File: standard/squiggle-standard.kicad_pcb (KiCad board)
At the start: 2 copper layers, 116 x 115.3 mm, 36 parts, among them SW1 switch, SW10 switch, SW11 switch, SW12 switch, SW13 switch, SW14 switch, SW15 switch, SW16 switch, SW17 switch, SW2 switch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

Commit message: minor thumb adjustments
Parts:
- SW13, SW17: footprint footprints:2u-dual -> footprints:1u-minimal
- moved D13 14.1 mm to (104.4, 88.0), turned to 73.4 degrees
- moved D17 13.9 mm to (110.1, 89.8)
- moved SW17 12.0 mm to (115.8, 95.5), turned to -26.6 degrees
- moved SW13 10.8 mm to (96.5, 87.9), turned to -16.6 degrees
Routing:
- removed copper zone on B.Cu, net (none)
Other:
- net class Default removed

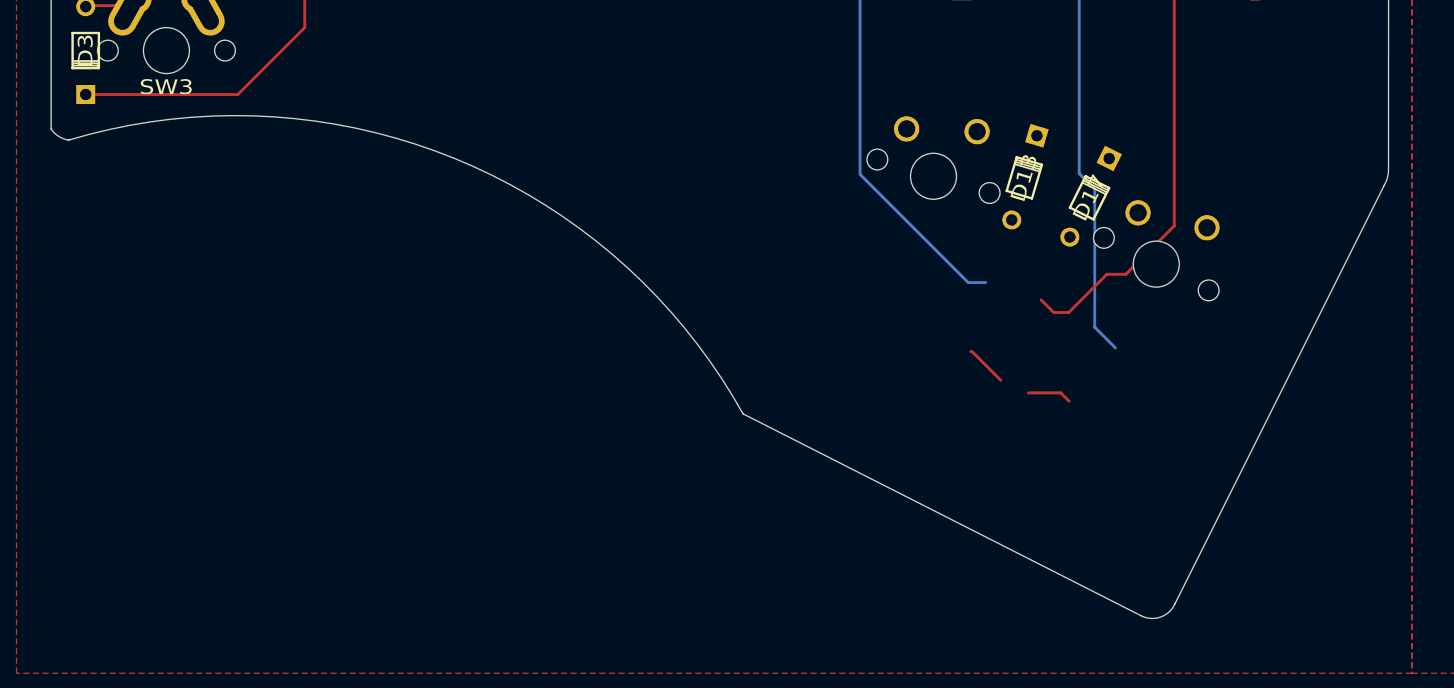
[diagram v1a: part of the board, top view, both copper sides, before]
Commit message: added placeholder for rotary encoder, swapped diodes orientations
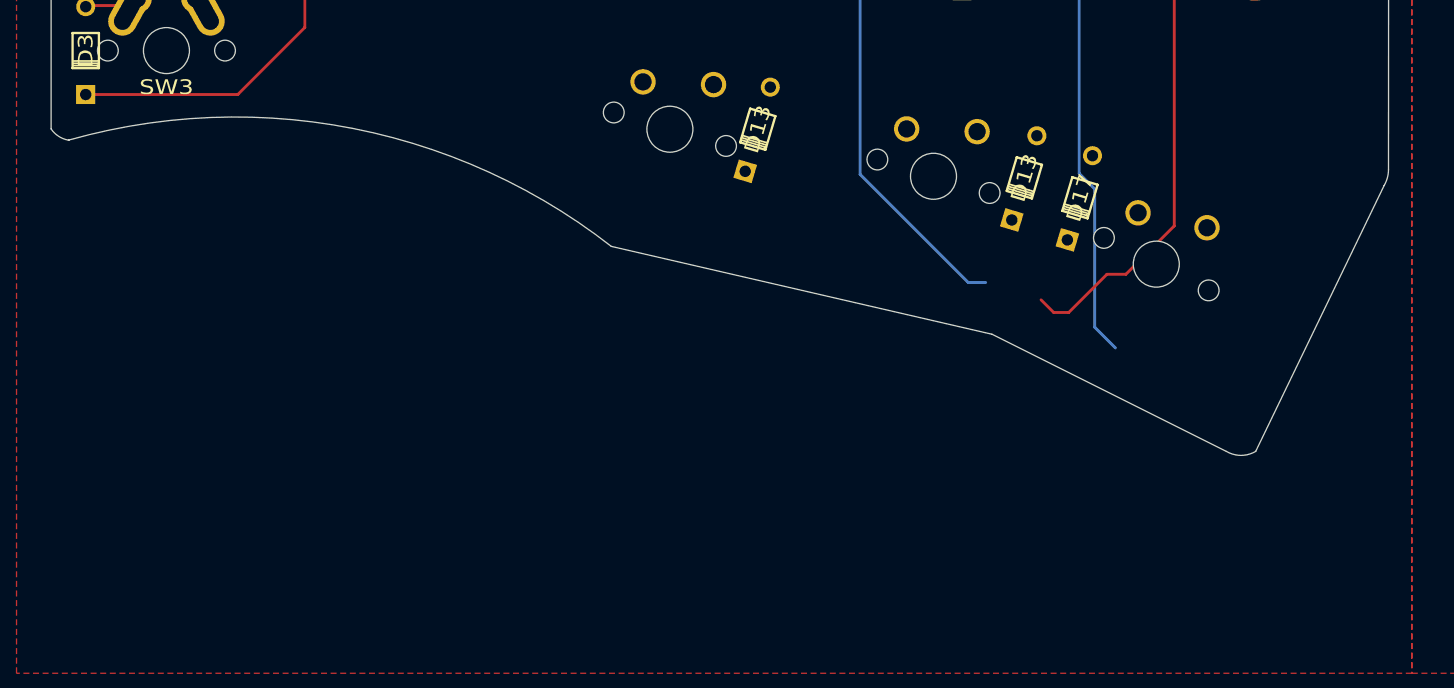
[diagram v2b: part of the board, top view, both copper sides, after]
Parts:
- added D13: D, footprints:diode, F.Cu at (81.3, 83.8)
- added SW13: switch, footprints:1u-minimal, F.Cu at (73.7, 83.8)
- moved D17 0.83 mm to (109.2, 89.8), turned to -106.6 degrees
- turned D13 to -106.6 degrees
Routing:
- net Net-(D17-Pad2): track 3.83 -> 0.00 mm
- net Net-(D13-Pad2): track 3.63 -> 0.00 mm
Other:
- board size 116 x 115.3 mm -> 116 x 101.2 mm
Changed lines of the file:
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@@
   )
   (footprint "footprints:diode" (layer "F.Cu")
-    (at 104.397119 88.037509 73.4)
+    (at 104.397119 88.037509 -106.6)
     (attr through_hole)
     (fp_text reference "D13" (at 0 0 73.4) (layer "F.SilkS")
@@
     (fp_line (start 1.3 1.1) (end 1.3 -1) (layer "F.SilkS") (width 0.15))
     (fp_line (start 0.9 1.1) (end 0.9 -1.1) (layer "F.SilkS") (width 0.15))
-    (pad "1" thru_hole rect locked (at 3.81 0 73.4) (size 1.651 1.651) (drill 0.9906) (layers *.Cu *.SilkS *.Mask)
+    (pad "1" thru_hole rect locked (at 3.81 0 253.4) (size 1.651 1.651) (drill 0.9906) (layers *.Cu *.SilkS *.Mask)
       (net 15 "ROW3"))
-    (pad "2" thru_hole circle locked (at -3.81 0 73.4) (size 1.651 1.651) (drill 0.9906) (layers *.Cu *.SilkS *.Mask)
+    (pad "2" thru_hole circle locked (at -3.81 0 253.4) (size 1.651 1.651) (drill 0.9906) (layers *.Cu *.SilkS *.Mask)
       (net 26 "Net-(D13-Pad2)"))
   )
   (footprint "footprints:diode" (layer "F.Cu")
-    (at 110.054038 89.766728 63.4)
-    (attr through_hole)
-    (fp_text reference "D17" (at 0 0 63.4) (layer "F.SilkS")
-      (effects (font (size 1.27 1.524) (thickness 0.2032)))
-    )
-    (fp_text value "D" (at 0 0 63.4) (layer "F.SilkS") hide
+    (at 109.22 89.766728 -106.6)
+    (attr through_hole)
+    (fp_text reference "D17" (at 0 0 73.4) (layer "F.SilkS")
+      (effects (font (size 1.27 1.524) (thickness 0.2032)))
+    )
+    (fp_text value "D" (at 0 0 73.4) (layer "F.SilkS") hide
       (effects (font (size 1.27 1.524) (thickness 0.2032)))
     )
@@
     (fp_line (start -1.524 -1.143) (end 1.524 -1.143) (layer "F.SilkS") (width 0.2032))
     (fp_line (start 0.9 1.1) (end 0.9 -1.1) (layer "F.SilkS") (width 0.15))
-    (pad "1" thru_hole rect locked (at 3.81 0 63.4) (size 1.651 1.651) (drill 0.9906) (layers *.Cu *.SilkS *.Mask)
+    (pad "1" thru_hole rect locked (at 3.81 0 253.4) (size 1.651 1.651) (drill 0.9906) (layers *.Cu *.SilkS *.Mask)
       (net 15 "ROW3"))
-    (pad "2" thru_hole circle locked (at -3.81 0 63.4) (size 1.651 1.651) (drill 0.9906) (layers *.Cu *.SilkS *.Mask)
+    (pad "2" thru_hole circle locked (at -3.81 0 253.4) (size 1.651 1.651) (drill 0.9906) (layers *.Cu *.SilkS *.Mask)
       (net 13 "Net-(D17-Pad2)"))
   )
@@
     (pad "2" thru_hole circle locked (at -3.81 0 270) (size 1.651 1.651) (drill 0.9906) (layers *.Cu *.SilkS *.Mask)
       (net 11 "Net-(D15-Pad2)"))
+  )
+  (footprint "footprints:1u-minimal" (layer "F.Cu")
+    (at 73.66 83.82 -16.6)
+    (attr through_hole)
+    (fp_text reference "SW13" (at 0 4 163.4) (layer "F.SilkS") hide
+      (effects (font (size 1.27 1.524) (thickness 0.2032)))
+    )
+    (fp_text value "switch" (at 0 5.8 163.4) (layer "F.SilkS") hide
+      (effects (font (size 1.27 1.524) (thickness 0.2032)))
+    )
+    (fp_text user "2.00u" (at -15.24 8.255 163.4) (layer "Dwgs.User")
+      (effects (font (size 1.524 1.524) (thickness 0.3048)))
+    )
+    (fp_line (start 9.5 9.5) (end -9.5 9.5) (layer "Dwgs.User") (width 0.1))
+    (fp_line (start -9.5 -9.5) (end 9.5 -9.5) (layer "Dwgs.User") (width 0.1))
+    (fp_line (start 9.5 -9.5) (end 9.5 9.5) (layer "Dwgs.User") (width 0.1))
+    (fp_line (start -9.5 9.5) (end -9.5 -9.5) (layer "Dwgs.User") (width 0.1))
+    (pad "" np_thru_hole circle locked (at 5.08 0 343.4) (size 1.8 1.8) (drill 1.8) (layers *.Cu *.Mask))
+    (pad "" np_thru_hole circle locked (at 0 0 343.4) (size 3.9878 3.9878) (drill 3.9878) (layers *.Cu *.Mask))
+    (pad "" np_thru_hole circle locked (at -5.08 0 343.4) (size 1.8 1.8) (drill 1.8) (layers *.Cu *.Mask))
+    (pad "1" thru_hole circle locked (at -3.405 -3.27 12.4) (size 2.2 2.2) (drill 1.5) (layers *.Cu *.Mask))
+    (pad "2" thru_hole circle locked (at 2.52 -4.79 343.4) (size 2.2 2.2) (drill 1.5) (layers *.Cu *.Mask))
+  )
+  (footprint "footprints:diode" (layer "F.Cu")
+    (at 81.28 83.82 -106.6)
+    (attr through_hole)
+    (fp_text reference "D13" (at 0 0 73.4) (layer "F.SilkS")
+      (effects (font (size 1.27 1.524) (thickness 0.2032)))
+    )
+    (fp_text value "D" (at 0 0 73.4) (layer "F.SilkS") hide
+      (effects (font (size 1.27 1.524) (thickness 0.2032)))
+    )
+    (fp_line (start 1.524 1.143) (end -1.524 1.143) (layer "B.SilkS") (width 0.2032))
+    (fp_line (start 1.524 -1.143) (end 1.524 1.143) (layer "B.SilkS") (width 0.2032))
+    (fp_line (start -1.524 -1.143) (end 1.524 -1.143) (layer "B.SilkS") (width 0.2032))
+    (fp_line (start 1.3 -1) (end 1.3 -1.1) (layer "B.SilkS") (width 0.15))
+    (fp_line (start 1.3 -1.1) (end 1.3 -1) (layer "B.SilkS") (width 0.15))
+    (fp_line (start 1.1 -1.1) (end 1.1 1.1) (layer "B.SilkS") (width 0.15))
+    (fp_line (start 0.9 1.1) (end 0.9 -1.1) (layer "B.SilkS") (width 0.15))
+    (fp_line (start 1.3 1.1) (end 1.3 -1) (layer "B.SilkS") (width 0.15))
+    (fp_line (start -1.524 1.143) (end -1.524 -1.143) (layer "B.SilkS") (width 0.2032))
+    (fp_line (start 1.524 -1.143) (end 1.524 1.143) (layer "F.SilkS") (width 0.2032))
+    (fp_line (start -1.524 -1.143) (end 1.524 -1.143) (layer "F.SilkS") (width 0.2032))
+    (fp_line (start 1.3 -1) (end 1.3 -1.1) (layer "F.SilkS") (width 0.15))
+    (fp_line (start -1.524 1.143) (end -1.524 -1.143) (layer "F.SilkS") (width 0.2032))
+    (fp_line (start 1.524 1.143) (end -1.524 1.143) (layer "F.SilkS") (width 0.2032))
+    (fp_line (start 1.1 -1.1) (end 1.1 1.1) (layer "F.SilkS") (width 0.15))
+    (fp_line (start 1.3 -1.1) (end 1.3 -1) (layer "F.SilkS") (width 0.15))
+    (fp_line (start 1.3 1.1) (end 1.3 -1) (layer "F.SilkS") (width 0.15))
+    (fp_line (start 0.9 1.1) (end 0.9 -1.1) (layer "F.SilkS") (width 0.15))
+    (pad "1" thru_hole rect locked (at 3.81 0 253.4) (size 1.651 1.651) (drill 0.9906) (layers *.Cu *.SilkS *.Mask))
+    (pad "2" thru_hole circle locked (at -3.81 0 253.4) (size 1.651 1.651) (drill 0.9906) (layers *.Cu *.SilkS *.Mask))
   )
   (footprint "footprints:trrs" (layer "B.Cu")
@@
   (gr_arc (start 21.499802 84.76712) (mid 20.652379 84.434796) (end 20.000001 83.799999) (layer "Edge.Cuts") (width 0.05))
   (gr_arc (start 135.978487 87.3) (mid 135.882196 88.025129) (end 135.599999 88.699999) (layer "Edge.Cuts") (width 0.05))
-  (gr_arc (start 117.457977 124.981089) (mid 116.199267 126.130029) (end 114.500001 125.999999) (layer "Edge.Cuts") (width 0.05))
   (gr_arc (start 21.027585 26.043499) (mid 67.853615 11.090172) (end 116 21) (layer "Edge.Cuts") (width 0.05))
   (gr_line (start 19.988572 27.759696) (end 20.000001 83.799999) (layer "Edge.Cuts") (width 0.05))
-  (gr_line (start 117.457977 124.981089) (end 135.6 88.7) (layer "Edge.Cuts") (width 0.05))
+  (gr_line (start 135.599999 88.699999) (end 124.46 111.76) (layer "Edge.Cuts") (width 0.05))
   (gr_line (start 135.978487 87.3) (end 136 22) (layer "Edge.Cuts") (width 0.05))
-  (gr_arc (start 21.591137 84.744072) (mid 54.973531 86.349651) (end 79.999999 108.500001) (layer "Edge.Cuts") (width 0.05))
+  (gr_line (start 121.92 111.76) (end 101.6 101.6) (layer "Edge.Cuts") (width 0.05))
+  (gr_arc (start 21.591137 84.744072) (mid 46.187759 83.754498) (end 68.58 93.98) (layer "Edge.Cuts") (width 0.05))
   (gr_arc (start 19.988572 27.759696) (mid 20.423138 26.850174) (end 21.027586 26.0435) (layer "Edge.Cuts") (width 0.05))
+  (gr_line (start 101.6 101.6) (end 68.58 93.98) (layer "Edge.Cuts") (width 0.05))
   (gr_arc (start 135 21) (mid 135.707107 21.292893) (end 136 22) (layer "Edge.Cuts") (width 0.05))
-  (gr_line (start 80 108.5) (end 114.5 126) (layer "Edge.Cuts") (width 0.05))
+  (gr_arc (start 124.46 111.76) (mid 123.19 112.105074) (end 121.92 111.76) (layer "Edge.Cuts") (width 0.05))
   (segment (start 23 35.1) (end 27.4 35.1) (width 0.25) (layer "F.Cu") (net 1))
   (segment (start 27.4 35.1) (end 27.5 35) (width 0.25) (layer "F.Cu") (net 1))
@@
   (segment (start 101.37 64.73) (end 102.845 64.73) (width 0.25) (layer "F.Cu") (net 12))
   (segment (start 103.4 64.1) (end 103.5 64) (width 0.25) (layer "F.Cu") (net 12))
-  (segment (start 107.567347 106.687202) (end 108.288648 107.408503) (width 0.25) (layer "F.Cu") (net 13))
-  (segment (start 104.75374 106.687202) (end 107.567347 106.687202) (width 0.25) (layer "F.Cu") (net 13))
   (segment (start 99 51.7345) (end 99 52.81) (width 0.25) (layer "F.Cu") (net 14))
   (segment (start 61 43.81) (end 74.0755 43.81) (width 0.25) (layer "F.Cu") (net 14))
@@
   (segment (start 65.4 55.1) (end 65.5 55) (width 0.25) (layer "F.Cu") (net 25))
   (segment (start 61 55.1) (end 65.4 55.1) (width 0.25) (layer "F.Cu") (net 25))
-  (segment (start 102.35374 105.587202) (end 99.864573 103.098035) (width 0.25) (layer "F.Cu") (net 26))
-  (segment (start 99.864573 103.098035) (end 99.754646 103.098035) (width 0.25) (layer "F.Cu") (net 26))
   (segment (start 103.4 26.1) (end 103.5 26) (width 0.25) (layer "F.Cu") (net 27))
   (segment (start 99 26.1) (end 103.4 26.1) (width 0.25) (layer "F.Cu") (net 27))

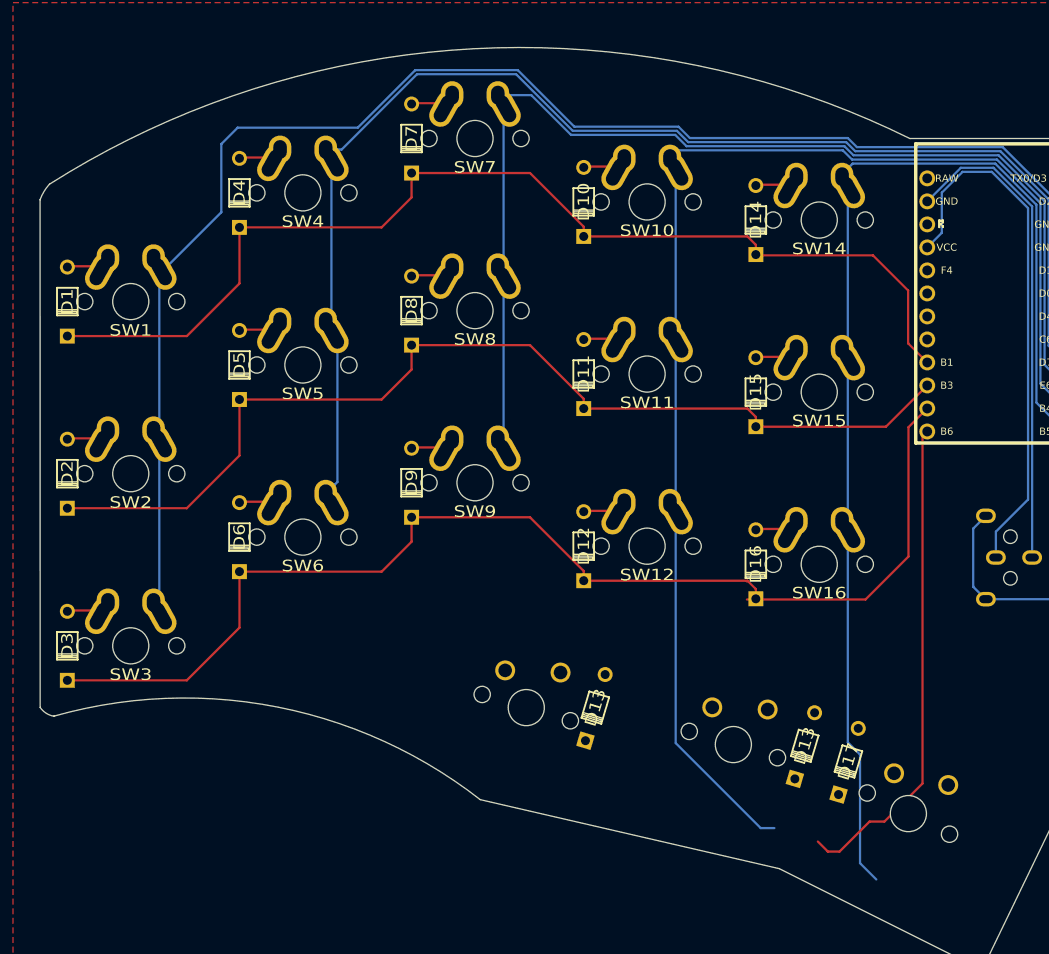
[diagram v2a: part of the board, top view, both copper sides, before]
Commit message: adding universal mx footprint, fixed column and row wiring, adjusted bottom left cut shape
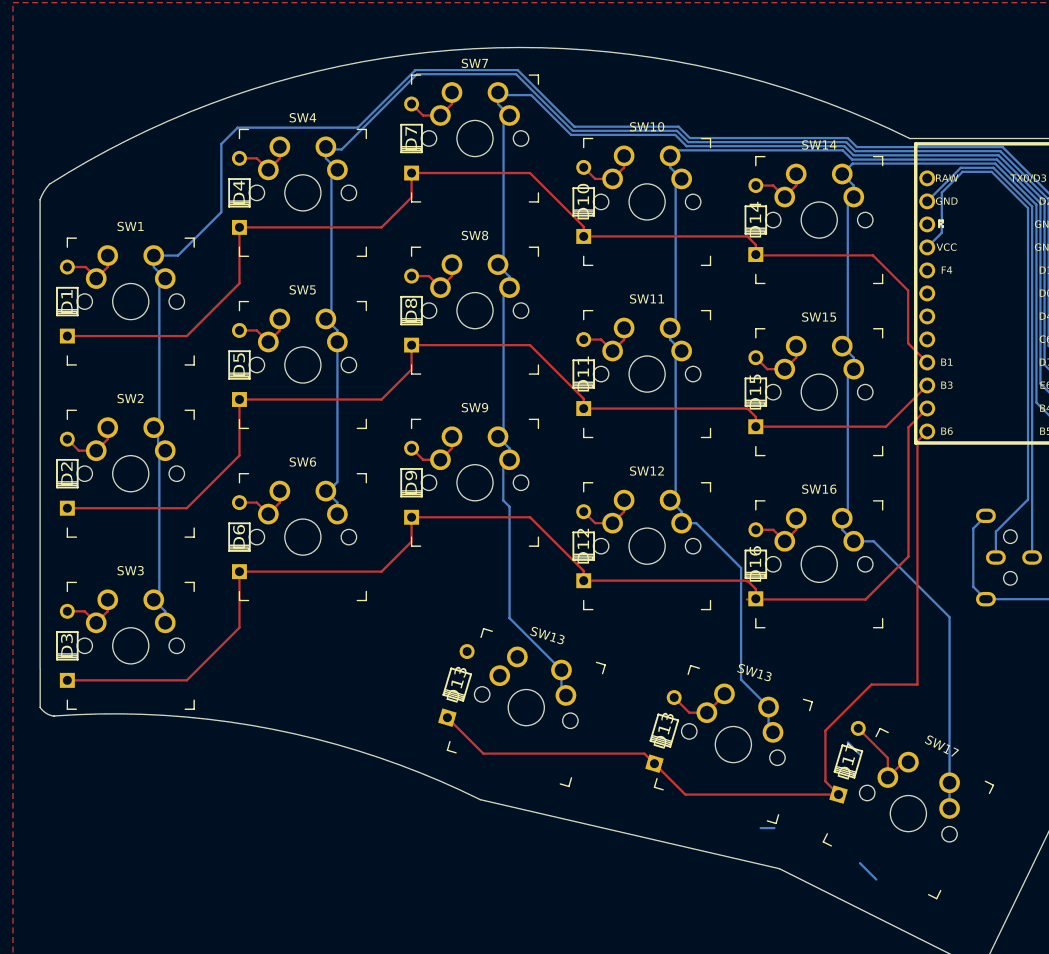
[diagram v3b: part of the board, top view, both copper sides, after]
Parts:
- SW1, SW10, SW11, SW12, SW14, SW15, SW16, SW2, SW3, SW4, SW5, SW6, SW7, SW8, SW9: footprint footprints:1u-dual -> footprints:SW_MX_reversible
- SW13 (x2), SW17: footprint footprints:1u-minimal -> footprints:SW_MX_reversible
- moved D13 15.6 mm to (88.9, 86.4)
- moved D13 15.5 mm to (66.0, 81.3)
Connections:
- D13 pad 1: (no net) -> ROW3
- D13 pad 2: (no net) -> Net-(D10-Pad2)
- SW13 pad 1: COL3 -> Net-(D13-Pad2)
- SW13 pad 2: Net-(D13-Pad2) -> COL3
- SW13 pad 1: (no net) -> Net-(D10-Pad2)
- SW13 pad 2: (no net) -> COL2
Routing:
- net ROW3: track 54.2 -> 95.0 mm
- net COL2: track 122.0 -> 159.8 mm
- net Net-(D17-Pad2): track 0.00 -> 9.76 mm
- net COL4: track 124.4 -> 133.8 mm
- net COL1: track 142.4 -> 151.6 mm
- net COL0: track 169.3 -> 177.9 mm
- net Net-(D13-Pad2): track 0.00 -> 7.17 mm
- net Net-(D2-Pad2): track 4.40 -> 6.78 mm
- net Net-(D3-Pad2): track 4.40 -> 6.78 mm
- net Net-(D14-Pad2): track 4.54 -> 6.78 mm
- net Net-(D7-Pad2): track 4.54 -> 6.78 mm
- net Net-(D10-Pad2): track 4.75 -> 6.78 mm
- net Net-(D15-Pad2): track 5.58 -> 6.78 mm
- net Net-(D1-Pad2): track 6.02 -> 7.13 mm
- net Net-(D5-Pad2): track 5.94 -> 6.78 mm
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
